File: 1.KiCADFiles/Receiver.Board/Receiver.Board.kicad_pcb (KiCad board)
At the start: 4 copper layers, 251 x 142 mm, 27 parts, among them J4 Conn_01x08, J5 Conn_Coaxial_Out, Q1 MMBT3904, Q2 MMBT3906

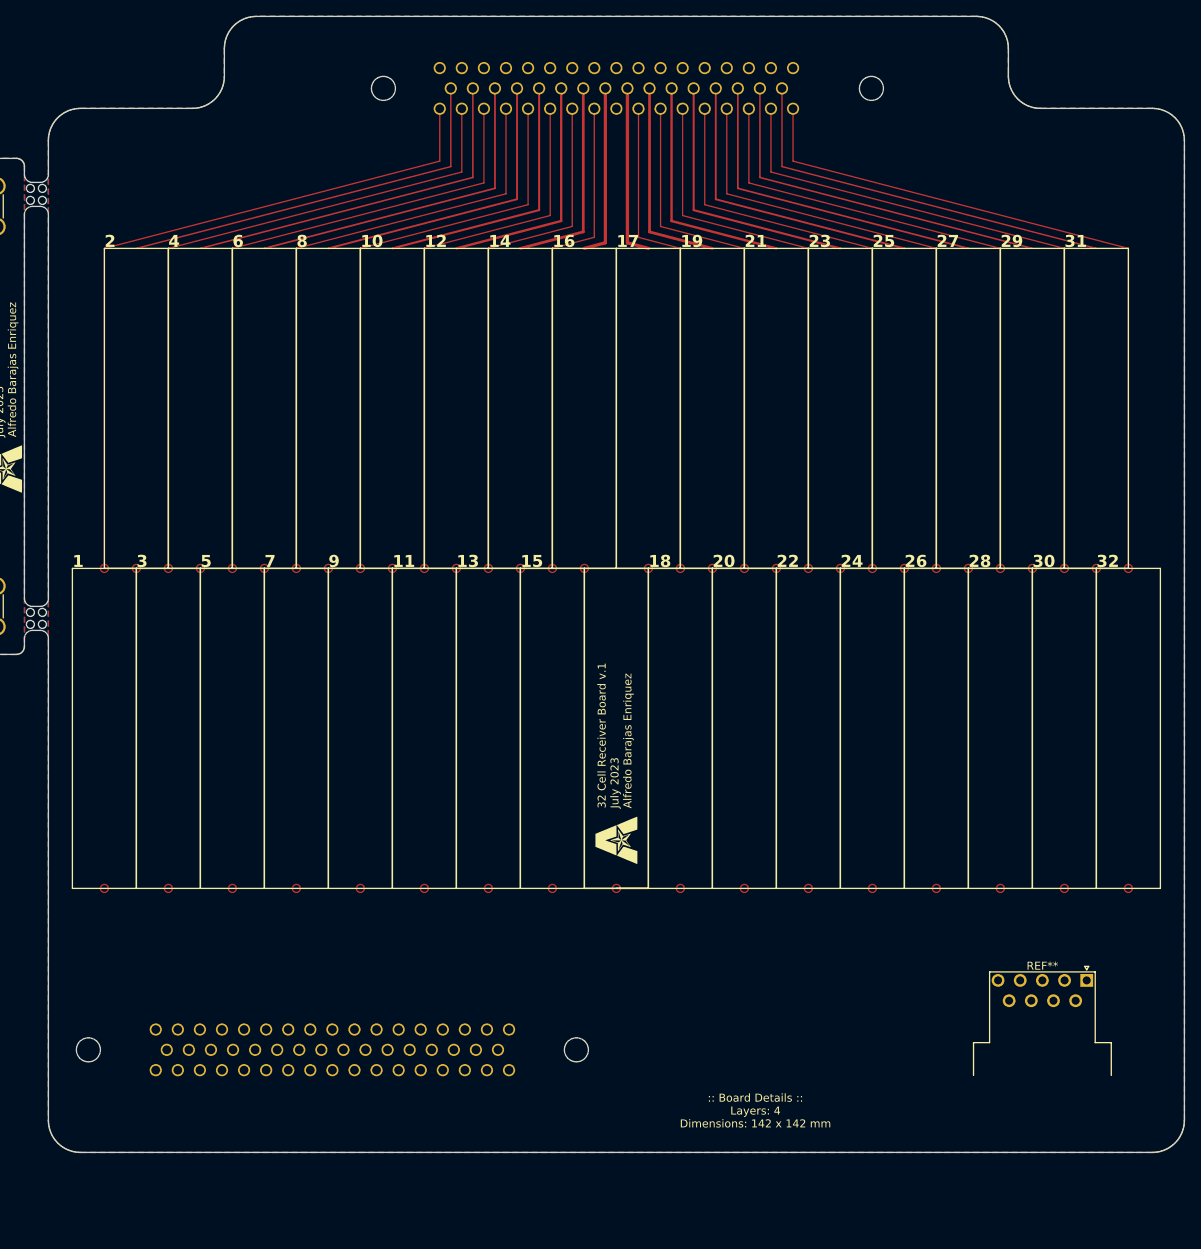
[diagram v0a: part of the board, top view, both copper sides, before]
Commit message: Started signal trace lines
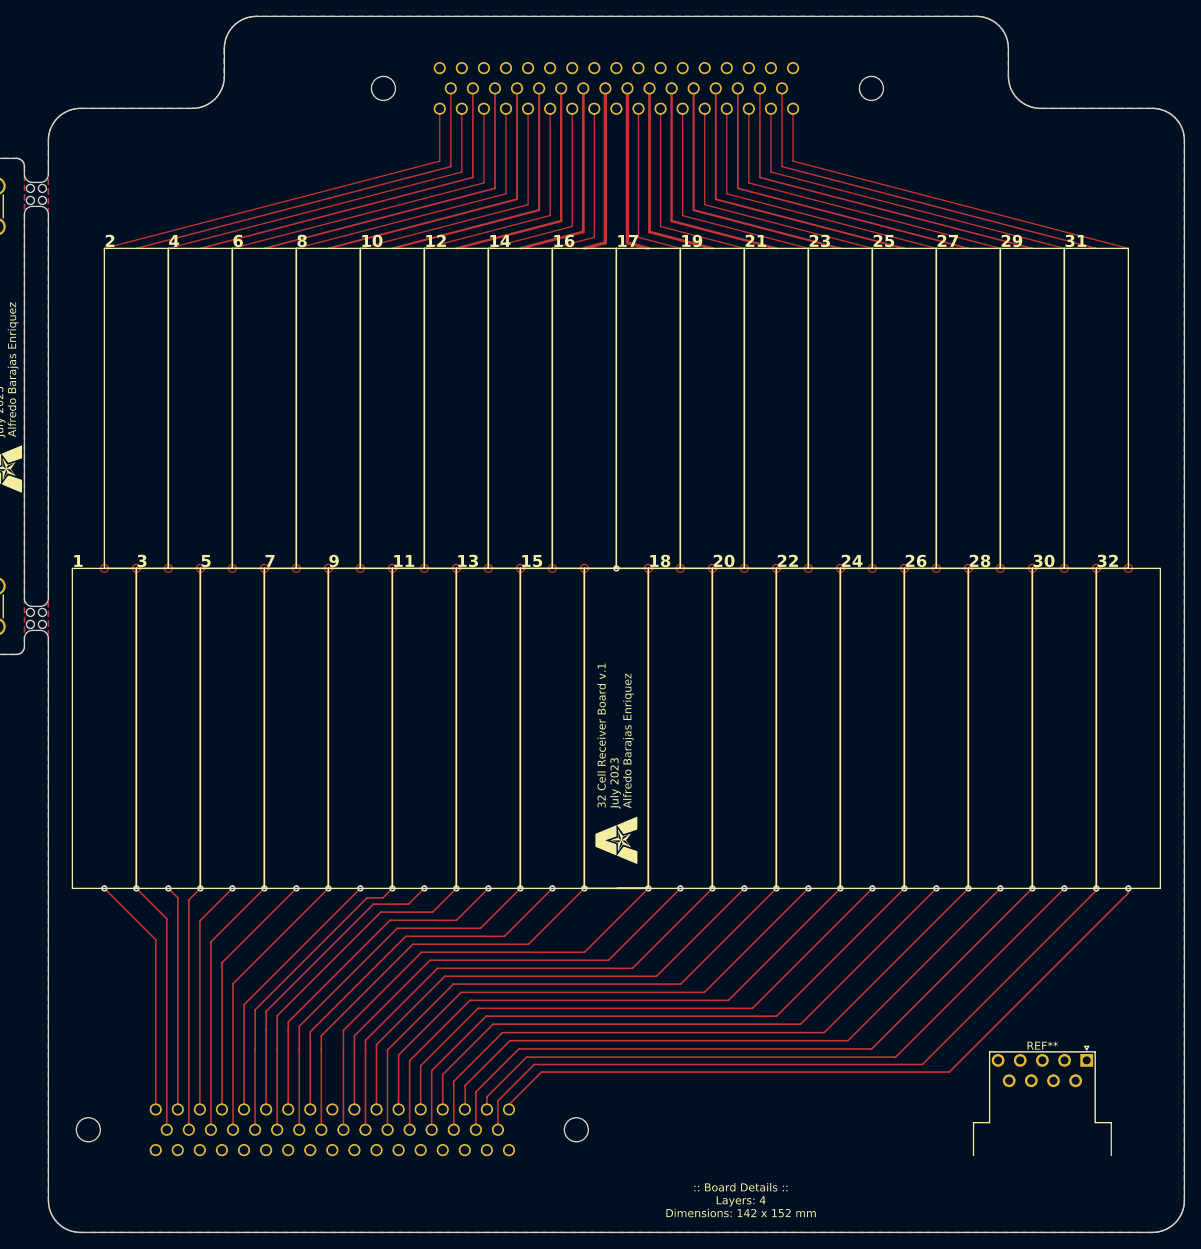
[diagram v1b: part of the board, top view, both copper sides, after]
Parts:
- moved REF** 10.0 mm to (258.8, 181.5)
- moved REF** 9.99 mm to (163.1, 190.2)
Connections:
- D1 pad 2: Net-(D1-A) -> +12
- D2 pad 1: Net-(D2-K) -> -12
- REF** pad 1: (no net) -> GND
- REF** pad 4: (no net) -> +12
- REF** pad 9: (no net) -> -12
- REF** pad 1: Net-(D1-A) -> +12
- REF** pad 3: Net-(D2-K) -> -12
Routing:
- net (no net): track 0.00 -> 1771.0 mm, vias 2 -> 34
- net Net-(D1-A): track 11.6 -> 0.00 mm
- net +12: track 0.00 -> 11.6 mm
- net Net-(D2-K): track 2.88 -> 0.00 mm
- net -12: track 0.00 -> 2.88 mm
- net GND1: vias 0 -> 1
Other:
- board size 251 x 142 mm -> 251 x 152 mm
- board text added: ":: Board Details :: Layers: 4 Dimensions: 142 x 152 mm"
- board text removed: ":: Board Details :: Layers: 4 Dimensions: 142 x 142 mm"

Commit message: Began adding signal traces, added cell holders
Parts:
- removed the REF** at (39.0, 122.1)
- removed the REF** at (39.0, 92.6)
- removed the REF** at (39.0, 89.6)
- removed the REF** at (39.0, 124.6)
- added REF**: PinSocket_1x03_P1.27mm_Vertical, Connector_PinSocket_1.27mm:PinSocket_1x03_P1.27mm_Vertical, F.Cu at (120.6, 114.5)
- added REF**: PinSocket_1x01_P1.27mm_Vertical, Connector_PinSocket_1.27mm:PinSocket_1x01_P1.27mm_Vertical, F.Cu at (120.6, 85.0)
- added REF**: PinSocket_1x01_P1.27mm_Vertical, Connector_PinSocket_1.27mm:PinSocket_1x01_P1.27mm_Vertical, F.Cu at (117.8, 82.5)
- added REF**: PinHeader_1x01_P1.27mm_Horizontal, Connector_PinHeader_1.27mm:PinHeader_1x01_P1.27mm_Horizontal, B.Cu at (39.0, 122.1)
- added REF**: PinHeader_1x03_P1.27mm_Horizontal, Connector_PinHeader_1.27mm:PinHeader_1x03_P1.27mm_Horizontal, B.Cu at (39.0, 95.2)
- added REF**: PinHeader_1x01_P1.27mm_Horizontal, Connector_PinHeader_1.27mm:PinHeader_1x01_P1.27mm_Horizontal, F.Cu at (39.0, 124.6)
- added REF**: PinSocket_1x01_P1.27mm_Vertical, Connector_PinSocket_1.27mm:PinSocket_1x01_P1.27mm_Vertical, F.Cu at (133.6, 157.5)
- added REF**: PinSocket_1x01_P1.27mm_Vertical, Connector_PinSocket_1.27mm:PinSocket_1x01_P1.27mm_Vertical, F.Cu at (136.5, 125.0)
- added REF**: PinSocket_1x01_P1.27mm_Vertical, Connector_PinSocket_1.27mm:PinSocket_1x01_P1.27mm_Vertical, F.Cu at (133.6, 122.5)
- added REF**: PinHeader_1x01_P1.27mm_Horizontal, Connector_PinHeader_1.27mm:PinHeader_1x01_P1.27mm_Horizontal, F.Cu at (39.0, 89.6)
- added REF**: PinSocket_1x01_P1.27mm_Vertical, Connector_PinSocket_1.27mm:PinSocket_1x01_P1.27mm_Vertical, F.Cu at (117.8, 117.5)
- added REF**: PinSocket_1x03_P1.27mm_Vertical, Connector_PinSocket_1.27mm:PinSocket_1x03_P1.27mm_Vertical, F.Cu at (136.5, 154.5)
- added REF**1: PinSocket_1x01_P1.27mm_Vertical, Connector_PinSocket_1.27mm:PinSocket_1x01_P1.27mm_Vertical, F.Cu at (141.6, 157.5)
- added REF**10: PinSocket_1x03_P1.27mm_Vertical, Connector_PinSocket_1.27mm:PinSocket_1x03_P1.27mm_Vertical, F.Cu at (160.5, 154.5)
- added REF**100: PinSocket_1x01_P1.27mm_Vertical, Connector_PinSocket_1.27mm:PinSocket_1x01_P1.27mm_Vertical, F.Cu at (201.6, 82.5)
- added REF**101: PinSocket_1x01_P1.27mm_Vertical, Connector_PinSocket_1.27mm:PinSocket_1x01_P1.27mm_Vertical, F.Cu at (209.6, 117.5)
- added REF**102: PinSocket_1x03_P1.27mm_Vertical, Connector_PinSocket_1.27mm:PinSocket_1x03_P1.27mm_Vertical, F.Cu at (212.5, 114.5)
- added REF**103: PinSocket_1x01_P1.27mm_Vertical, Connector_PinSocket_1.27mm:PinSocket_1x01_P1.27mm_Vertical, F.Cu at (212.5, 85.0)
- added REF**104: PinSocket_1x01_P1.27mm_Vertical, Connector_PinSocket_1.27mm:PinSocket_1x01_P1.27mm_Vertical, F.Cu at (209.6, 82.5)
- added REF**105: PinSocket_1x01_P1.27mm_Vertical, Connector_PinSocket_1.27mm:PinSocket_1x01_P1.27mm_Vertical, F.Cu at (217.6, 117.5)
- added REF**106: PinSocket_1x03_P1.27mm_Vertical, Connector_PinSocket_1.27mm:PinSocket_1x03_P1.27mm_Vertical, F.Cu at (220.5, 114.5)
- added REF**107: PinSocket_1x01_P1.27mm_Vertical, Connector_PinSocket_1.27mm:PinSocket_1x01_P1.27mm_Vertical, F.Cu at (220.5, 85.0)
- added REF**108: PinSocket_1x01_P1.27mm_Vertical, Connector_PinSocket_1.27mm:PinSocket_1x01_P1.27mm_Vertical, F.Cu at (217.6, 82.5)
- added REF**109: PinSocket_1x01_P1.27mm_Vertical, Connector_PinSocket_1.27mm:PinSocket_1x01_P1.27mm_Vertical, F.Cu at (225.6, 117.5)
- added REF**11: PinSocket_1x01_P1.27mm_Vertical, Connector_PinSocket_1.27mm:PinSocket_1x01_P1.27mm_Vertical, F.Cu at (160.5, 125.0)
- added REF**110: PinSocket_1x03_P1.27mm_Vertical, Connector_PinSocket_1.27mm:PinSocket_1x03_P1.27mm_Vertical, F.Cu at (228.5, 114.5)
- added REF**111: PinSocket_1x01_P1.27mm_Vertical, Connector_PinSocket_1.27mm:PinSocket_1x01_P1.27mm_Vertical, F.Cu at (228.5, 85.0)
- added REF**112: PinSocket_1x01_P1.27mm_Vertical, Connector_PinSocket_1.27mm:PinSocket_1x01_P1.27mm_Vertical, F.Cu at (225.6, 82.5)
- added REF**113: PinSocket_1x01_P1.27mm_Vertical, Connector_PinSocket_1.27mm:PinSocket_1x01_P1.27mm_Vertical, F.Cu at (233.6, 117.5)
- added REF**114: PinSocket_1x03_P1.27mm_Vertical, Connector_PinSocket_1.27mm:PinSocket_1x03_P1.27mm_Vertical, F.Cu at (236.5, 114.5)
- added REF**115: PinSocket_1x01_P1.27mm_Vertical, Connector_PinSocket_1.27mm:PinSocket_1x01_P1.27mm_Vertical, F.Cu at (236.5, 85.0)
- added REF**116: PinSocket_1x01_P1.27mm_Vertical, Connector_PinSocket_1.27mm:PinSocket_1x01_P1.27mm_Vertical, F.Cu at (233.6, 82.5)
- added REF**117: PinSocket_1x01_P1.27mm_Vertical, Connector_PinSocket_1.27mm:PinSocket_1x01_P1.27mm_Vertical, F.Cu at (241.6, 117.5)
- added REF**118: PinSocket_1x03_P1.27mm_Vertical, Connector_PinSocket_1.27mm:PinSocket_1x03_P1.27mm_Vertical, F.Cu at (244.5, 114.5)
- added REF**119: PinSocket_1x01_P1.27mm_Vertical, Connector_PinSocket_1.27mm:PinSocket_1x01_P1.27mm_Vertical, F.Cu at (244.5, 85.0)
- added REF**12: PinSocket_1x01_P1.27mm_Vertical, Connector_PinSocket_1.27mm:PinSocket_1x01_P1.27mm_Vertical, F.Cu at (157.6, 122.5)
- added REF**120: PinSocket_1x01_P1.27mm_Vertical, Connector_PinSocket_1.27mm:PinSocket_1x01_P1.27mm_Vertical, F.Cu at (241.6, 82.5)
- added REF**121: PinSocket_1x01_P1.27mm_Vertical, Connector_PinSocket_1.27mm:PinSocket_1x01_P1.27mm_Vertical, F.Cu at (249.6, 117.5)
- added REF**122: PinSocket_1x03_P1.27mm_Vertical, Connector_PinSocket_1.27mm:PinSocket_1x03_P1.27mm_Vertical, F.Cu at (252.5, 114.5)
- added REF**123: PinSocket_1x01_P1.27mm_Vertical, Connector_PinSocket_1.27mm:PinSocket_1x01_P1.27mm_Vertical, F.Cu at (252.5, 85.0)
- added REF**124: PinSocket_1x01_P1.27mm_Vertical, Connector_PinSocket_1.27mm:PinSocket_1x01_P1.27mm_Vertical, F.Cu at (249.6, 82.5)
- added REF**125: PinSocket_1x01_P1.27mm_Vertical, Connector_PinSocket_1.27mm:PinSocket_1x01_P1.27mm_Vertical, F.Cu at (257.6, 117.5)
- added REF**126: PinSocket_1x03_P1.27mm_Vertical, Connector_PinSocket_1.27mm:PinSocket_1x03_P1.27mm_Vertical, F.Cu at (260.5, 114.5)
- added REF**127: PinSocket_1x01_P1.27mm_Vertical, Connector_PinSocket_1.27mm:PinSocket_1x01_P1.27mm_Vertical, F.Cu at (260.5, 85.0)
- added REF**128: PinSocket_1x01_P1.27mm_Vertical, Connector_PinSocket_1.27mm:PinSocket_1x01_P1.27mm_Vertical, F.Cu at (257.6, 82.5)
- added REF**13: PinSocket_1x01_P1.27mm_Vertical, Connector_PinSocket_1.27mm:PinSocket_1x01_P1.27mm_Vertical, F.Cu at (165.6, 157.5)
- added REF**14: PinSocket_1x03_P1.27mm_Vertical, Connector_PinSocket_1.27mm:PinSocket_1x03_P1.27mm_Vertical, F.Cu at (168.5, 154.5)
- added REF**15: PinSocket_1x01_P1.27mm_Vertical, Connector_PinSocket_1.27mm:PinSocket_1x01_P1.27mm_Vertical, F.Cu at (168.5, 125.0)
- added REF**16: PinSocket_1x01_P1.27mm_Vertical, Connector_PinSocket_1.27mm:PinSocket_1x01_P1.27mm_Vertical, F.Cu at (165.6, 122.5)
- added REF**17: PinSocket_1x01_P1.27mm_Vertical, Connector_PinSocket_1.27mm:PinSocket_1x01_P1.27mm_Vertical, F.Cu at (173.6, 157.5)
- added REF**18: PinSocket_1x03_P1.27mm_Vertical, Connector_PinSocket_1.27mm:PinSocket_1x03_P1.27mm_Vertical, F.Cu at (176.5, 154.5)
- added REF**19: PinSocket_1x01_P1.27mm_Vertical, Connector_PinSocket_1.27mm:PinSocket_1x01_P1.27mm_Vertical, F.Cu at (176.5, 125.0)
- added REF**2: PinSocket_1x03_P1.27mm_Vertical, Connector_PinSocket_1.27mm:PinSocket_1x03_P1.27mm_Vertical, F.Cu at (144.5, 154.5)
- added REF**20: PinSocket_1x01_P1.27mm_Vertical, Connector_PinSocket_1.27mm:PinSocket_1x01_P1.27mm_Vertical, F.Cu at (173.6, 122.5)
- added REF**21: PinSocket_1x01_P1.27mm_Vertical, Connector_PinSocket_1.27mm:PinSocket_1x01_P1.27mm_Vertical, F.Cu at (181.6, 157.5)
- added REF**22: PinSocket_1x03_P1.27mm_Vertical, Connector_PinSocket_1.27mm:PinSocket_1x03_P1.27mm_Vertical, F.Cu at (184.5, 154.5)
- added REF**23: PinSocket_1x01_P1.27mm_Vertical, Connector_PinSocket_1.27mm:PinSocket_1x01_P1.27mm_Vertical, F.Cu at (184.5, 125.0)
- added REF**24: PinSocket_1x01_P1.27mm_Vertical, Connector_PinSocket_1.27mm:PinSocket_1x01_P1.27mm_Vertical, F.Cu at (181.6, 122.5)
- added REF**25: PinSocket_1x01_P1.27mm_Vertical, Connector_PinSocket_1.27mm:PinSocket_1x01_P1.27mm_Vertical, F.Cu at (189.6, 157.5)
- added REF**26: PinSocket_1x03_P1.27mm_Vertical, Connector_PinSocket_1.27mm:PinSocket_1x03_P1.27mm_Vertical, F.Cu at (192.5, 154.5)
- added REF**27: PinSocket_1x01_P1.27mm_Vertical, Connector_PinSocket_1.27mm:PinSocket_1x01_P1.27mm_Vertical, F.Cu at (192.5, 125.0)
- added REF**28: PinSocket_1x01_P1.27mm_Vertical, Connector_PinSocket_1.27mm:PinSocket_1x01_P1.27mm_Vertical, F.Cu at (189.6, 122.5)
- added REF**3: PinSocket_1x01_P1.27mm_Vertical, Connector_PinSocket_1.27mm:PinSocket_1x01_P1.27mm_Vertical, F.Cu at (144.5, 125.0)
- added REF**33: PinSocket_1x01_P1.27mm_Vertical, Connector_PinSocket_1.27mm:PinSocket_1x01_P1.27mm_Vertical, F.Cu at (205.6, 157.5)
- added REF**34: PinSocket_1x03_P1.27mm_Vertical, Connector_PinSocket_1.27mm:PinSocket_1x03_P1.27mm_Vertical, F.Cu at (208.5, 154.5)
- added REF**35: PinSocket_1x01_P1.27mm_Vertical, Connector_PinSocket_1.27mm:PinSocket_1x01_P1.27mm_Vertical, F.Cu at (208.5, 125.0)
- added REF**36: PinSocket_1x01_P1.27mm_Vertical, Connector_PinSocket_1.27mm:PinSocket_1x01_P1.27mm_Vertical, F.Cu at (205.6, 122.5)
- added REF**37: PinSocket_1x01_P1.27mm_Vertical, Connector_PinSocket_1.27mm:PinSocket_1x01_P1.27mm_Vertical, F.Cu at (213.6, 157.5)
- added REF**38: PinSocket_1x03_P1.27mm_Vertical, Connector_PinSocket_1.27mm:PinSocket_1x03_P1.27mm_Vertical, F.Cu at (216.5, 154.5)
- added REF**39: PinSocket_1x01_P1.27mm_Vertical, Connector_PinSocket_1.27mm:PinSocket_1x01_P1.27mm_Vertical, F.Cu at (216.5, 125.0)
- added REF**4: PinSocket_1x01_P1.27mm_Vertical, Connector_PinSocket_1.27mm:PinSocket_1x01_P1.27mm_Vertical, F.Cu at (141.6, 122.5)
- added REF**40: PinSocket_1x01_P1.27mm_Vertical, Connector_PinSocket_1.27mm:PinSocket_1x01_P1.27mm_Vertical, F.Cu at (213.6, 122.5)
- added REF**41: PinSocket_1x01_P1.27mm_Vertical, Connector_PinSocket_1.27mm:PinSocket_1x01_P1.27mm_Vertical, F.Cu at (221.6, 157.5)
- added REF**42: PinSocket_1x03_P1.27mm_Vertical, Connector_PinSocket_1.27mm:PinSocket_1x03_P1.27mm_Vertical, F.Cu at (224.5, 154.5)
- added REF**43: PinSocket_1x01_P1.27mm_Vertical, Connector_PinSocket_1.27mm:PinSocket_1x01_P1.27mm_Vertical, F.Cu at (224.5, 125.0)
- added REF**44: PinSocket_1x01_P1.27mm_Vertical, Connector_PinSocket_1.27mm:PinSocket_1x01_P1.27mm_Vertical, F.Cu at (221.6, 122.5)
- added REF**45: PinSocket_1x01_P1.27mm_Vertical, Connector_PinSocket_1.27mm:PinSocket_1x01_P1.27mm_Vertical, F.Cu at (229.6, 157.5)
- added REF**46: PinSocket_1x03_P1.27mm_Vertical, Connector_PinSocket_1.27mm:PinSocket_1x03_P1.27mm_Vertical, F.Cu at (232.5, 154.5)
- added REF**47: PinSocket_1x01_P1.27mm_Vertical, Connector_PinSocket_1.27mm:PinSocket_1x01_P1.27mm_Vertical, F.Cu at (232.5, 125.0)
- added REF**48: PinSocket_1x01_P1.27mm_Vertical, Connector_PinSocket_1.27mm:PinSocket_1x01_P1.27mm_Vertical, F.Cu at (229.6, 122.5)
- added REF**49: PinSocket_1x01_P1.27mm_Vertical, Connector_PinSocket_1.27mm:PinSocket_1x01_P1.27mm_Vertical, F.Cu at (237.6, 157.5)
- added REF**5: PinSocket_1x01_P1.27mm_Vertical, Connector_PinSocket_1.27mm:PinSocket_1x01_P1.27mm_Vertical, F.Cu at (149.6, 157.5)
- added REF**50: PinSocket_1x03_P1.27mm_Vertical, Connector_PinSocket_1.27mm:PinSocket_1x03_P1.27mm_Vertical, F.Cu at (240.5, 154.5)
- added REF**51: PinSocket_1x01_P1.27mm_Vertical, Connector_PinSocket_1.27mm:PinSocket_1x01_P1.27mm_Vertical, F.Cu at (240.5, 125.0)
- added REF**52: PinSocket_1x01_P1.27mm_Vertical, Connector_PinSocket_1.27mm:PinSocket_1x01_P1.27mm_Vertical, F.Cu at (237.6, 122.5)
- added REF**53: PinSocket_1x01_P1.27mm_Vertical, Connector_PinSocket_1.27mm:PinSocket_1x01_P1.27mm_Vertical, F.Cu at (245.6, 157.5)
- added REF**54: PinSocket_1x03_P1.27mm_Vertical, Connector_PinSocket_1.27mm:PinSocket_1x03_P1.27mm_Vertical, F.Cu at (248.5, 154.5)
- added REF**55: PinSocket_1x01_P1.27mm_Vertical, Connector_PinSocket_1.27mm:PinSocket_1x01_P1.27mm_Vertical, F.Cu at (248.5, 125.0)
- added REF**56: PinSocket_1x01_P1.27mm_Vertical, Connector_PinSocket_1.27mm:PinSocket_1x01_P1.27mm_Vertical, F.Cu at (245.6, 122.5)
- added REF**57: PinSocket_1x01_P1.27mm_Vertical, Connector_PinSocket_1.27mm:PinSocket_1x01_P1.27mm_Vertical, F.Cu at (253.6, 157.5)
- added REF**58: PinSocket_1x03_P1.27mm_Vertical, Connector_PinSocket_1.27mm:PinSocket_1x03_P1.27mm_Vertical, F.Cu at (256.5, 154.5)
- added REF**59: PinSocket_1x01_P1.27mm_Vertical, Connector_PinSocket_1.27mm:PinSocket_1x01_P1.27mm_Vertical, F.Cu at (256.5, 125.0)
- added REF**6: PinSocket_1x03_P1.27mm_Vertical, Connector_PinSocket_1.27mm:PinSocket_1x03_P1.27mm_Vertical, F.Cu at (152.5, 154.5)
- added REF**60: PinSocket_1x01_P1.27mm_Vertical, Connector_PinSocket_1.27mm:PinSocket_1x01_P1.27mm_Vertical, F.Cu at (253.6, 122.5)
- added REF**61: PinSocket_1x01_P1.27mm_Vertical, Connector_PinSocket_1.27mm:PinSocket_1x01_P1.27mm_Vertical, F.Cu at (261.6, 157.5)
- added REF**62: PinSocket_1x03_P1.27mm_Vertical, Connector_PinSocket_1.27mm:PinSocket_1x03_P1.27mm_Vertical, F.Cu at (264.5, 154.5)
- added REF**63: PinSocket_1x01_P1.27mm_Vertical, Connector_PinSocket_1.27mm:PinSocket_1x01_P1.27mm_Vertical, F.Cu at (264.5, 125.0)
- added REF**64: PinSocket_1x01_P1.27mm_Vertical, Connector_PinSocket_1.27mm:PinSocket_1x01_P1.27mm_Vertical, F.Cu at (261.6, 122.5)
- added REF**65: PinSocket_1x01_P1.27mm_Vertical, Connector_PinSocket_1.27mm:PinSocket_1x01_P1.27mm_Vertical, F.Cu at (137.6, 117.5)
- added REF**66: PinSocket_1x03_P1.27mm_Vertical, Connector_PinSocket_1.27mm:PinSocket_1x03_P1.27mm_Vertical, F.Cu at (140.5, 114.5)
- added REF**67: PinSocket_1x01_P1.27mm_Vertical, Connector_PinSocket_1.27mm:PinSocket_1x01_P1.27mm_Vertical, F.Cu at (140.5, 85.0)
- added REF**68: PinSocket_1x01_P1.27mm_Vertical, Connector_PinSocket_1.27mm:PinSocket_1x01_P1.27mm_Vertical, F.Cu at (137.6, 82.5)
- added REF**69: PinSocket_1x01_P1.27mm_Vertical, Connector_PinSocket_1.27mm:PinSocket_1x01_P1.27mm_Vertical, F.Cu at (145.6, 117.5)
- added REF**7: PinSocket_1x01_P1.27mm_Vertical, Connector_PinSocket_1.27mm:PinSocket_1x01_P1.27mm_Vertical, F.Cu at (152.5, 125.0)
- added REF**70: PinSocket_1x03_P1.27mm_Vertical, Connector_PinSocket_1.27mm:PinSocket_1x03_P1.27mm_Vertical, F.Cu at (148.5, 114.5)
- added REF**71: PinSocket_1x01_P1.27mm_Vertical, Connector_PinSocket_1.27mm:PinSocket_1x01_P1.27mm_Vertical, F.Cu at (148.5, 85.0)
- added REF**72: PinSocket_1x01_P1.27mm_Vertical, Connector_PinSocket_1.27mm:PinSocket_1x01_P1.27mm_Vertical, F.Cu at (145.6, 82.5)
- added REF**73: PinSocket_1x01_P1.27mm_Vertical, Connector_PinSocket_1.27mm:PinSocket_1x01_P1.27mm_Vertical, F.Cu at (153.6, 117.5)
- added REF**74: PinSocket_1x03_P1.27mm_Vertical, Connector_PinSocket_1.27mm:PinSocket_1x03_P1.27mm_Vertical, F.Cu at (156.5, 114.5)
- added REF**75: PinSocket_1x01_P1.27mm_Vertical, Connector_PinSocket_1.27mm:PinSocket_1x01_P1.27mm_Vertical, F.Cu at (156.5, 85.0)
- added REF**76: PinSocket_1x01_P1.27mm_Vertical, Connector_PinSocket_1.27mm:PinSocket_1x01_P1.27mm_Vertical, F.Cu at (153.6, 82.5)
- added REF**77: PinSocket_1x01_P1.27mm_Vertical, Connector_PinSocket_1.27mm:PinSocket_1x01_P1.27mm_Vertical, F.Cu at (161.6, 117.5)
- added REF**78: PinSocket_1x03_P1.27mm_Vertical, Connector_PinSocket_1.27mm:PinSocket_1x03_P1.27mm_Vertical, F.Cu at (164.5, 114.5)
- added REF**79: PinSocket_1x01_P1.27mm_Vertical, Connector_PinSocket_1.27mm:PinSocket_1x01_P1.27mm_Vertical, F.Cu at (164.5, 85.0)
- added REF**8: PinSocket_1x01_P1.27mm_Vertical, Connector_PinSocket_1.27mm:PinSocket_1x01_P1.27mm_Vertical, F.Cu at (149.6, 122.5)
- added REF**80: PinSocket_1x01_P1.27mm_Vertical, Connector_PinSocket_1.27mm:PinSocket_1x01_P1.27mm_Vertical, F.Cu at (161.6, 82.5)
- added REF**81: PinSocket_1x01_P1.27mm_Vertical, Connector_PinSocket_1.27mm:PinSocket_1x01_P1.27mm_Vertical, F.Cu at (169.6, 117.5)
- added REF**82: PinSocket_1x03_P1.27mm_Vertical, Connector_PinSocket_1.27mm:PinSocket_1x03_P1.27mm_Vertical, F.Cu at (172.5, 114.5)
- added REF**83: PinSocket_1x01_P1.27mm_Vertical, Connector_PinSocket_1.27mm:PinSocket_1x01_P1.27mm_Vertical, F.Cu at (172.5, 85.0)
- added REF**84: PinSocket_1x01_P1.27mm_Vertical, Connector_PinSocket_1.27mm:PinSocket_1x01_P1.27mm_Vertical, F.Cu at (169.6, 82.5)
- added REF**85: PinSocket_1x01_P1.27mm_Vertical, Connector_PinSocket_1.27mm:PinSocket_1x01_P1.27mm_Vertical, F.Cu at (177.6, 117.5)
- added REF**86: PinSocket_1x03_P1.27mm_Vertical, Connector_PinSocket_1.27mm:PinSocket_1x03_P1.27mm_Vertical, F.Cu at (180.5, 114.5)
- added REF**87: PinSocket_1x01_P1.27mm_Vertical, Connector_PinSocket_1.27mm:PinSocket_1x01_P1.27mm_Vertical, F.Cu at (180.5, 85.0)
- added REF**88: PinSocket_1x01_P1.27mm_Vertical, Connector_PinSocket_1.27mm:PinSocket_1x01_P1.27mm_Vertical, F.Cu at (177.6, 82.5)
- added REF**89: PinSocket_1x01_P1.27mm_Vertical, Connector_PinSocket_1.27mm:PinSocket_1x01_P1.27mm_Vertical, F.Cu at (185.6, 117.5)
- added REF**9: PinSocket_1x01_P1.27mm_Vertical, Connector_PinSocket_1.27mm:PinSocket_1x01_P1.27mm_Vertical, F.Cu at (157.6, 157.5)
- added REF**90: PinSocket_1x03_P1.27mm_Vertical, Connector_PinSocket_1.27mm:PinSocket_1x03_P1.27mm_Vertical, F.Cu at (188.5, 114.5)
- added REF**91: PinSocket_1x01_P1.27mm_Vertical, Connector_PinSocket_1.27mm:PinSocket_1x01_P1.27mm_Vertical, F.Cu at (188.5, 85.0)
- added REF**92: PinSocket_1x01_P1.27mm_Vertical, Connector_PinSocket_1.27mm:PinSocket_1x01_P1.27mm_Vertical, F.Cu at (185.6, 82.5)
- added REF**93: PinSocket_1x01_P1.27mm_Vertical, Connector_PinSocket_1.27mm:PinSocket_1x01_P1.27mm_Vertical, F.Cu at (193.6, 117.5)
- added REF**94: PinSocket_1x03_P1.27mm_Vertical, Connector_PinSocket_1.27mm:PinSocket_1x03_P1.27mm_Vertical, F.Cu at (196.5, 114.5)
- added REF**95: PinSocket_1x01_P1.27mm_Vertical, Connector_PinSocket_1.27mm:PinSocket_1x01_P1.27mm_Vertical, F.Cu at (196.5, 85.0)
- added REF**96: PinSocket_1x01_P1.27mm_Vertical, Connector_PinSocket_1.27mm:PinSocket_1x01_P1.27mm_Vertical, F.Cu at (193.6, 82.5)
- added REF**97: PinSocket_1x01_P1.27mm_Vertical, Connector_PinSocket_1.27mm:PinSocket_1x01_P1.27mm_Vertical, F.Cu at (201.6, 117.5)
- added REF**98: PinSocket_1x03_P1.27mm_Vertical, Connector_PinSocket_1.27mm:PinSocket_1x03_P1.27mm_Vertical, F.Cu at (204.5, 114.5)
- added REF**99: PinSocket_1x01_P1.27mm_Vertical, Connector_PinSocket_1.27mm:PinSocket_1x01_P1.27mm_Vertical, F.Cu at (204.5, 85.0)
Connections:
- REF** pad 1: (no net) -> GND
- REF** pad 4: (no net) -> +12
- REF** pad 8: (no net) -> -12
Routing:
- net (no net): track 1771.0 -> 1813.1 mm, vias 34 -> 2
- net +12: track 11.6 -> 41.9 mm
- net -12: track 2.88 -> 28.6 mm

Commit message: Fixed cell board orientation, routed power lines, fixed wire capacitance with new lengths, updated excel sheet to include all traces
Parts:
- removed C1, C2, C3, C4: 10uF, Capacitor_SMD:C_1206_3216Metric_Pad1.33x1.80mm_HandSolder
- removed D1, D2: 1N4148W, Diode_SMD:D_SOD-123
- removed D3, D4: BZV55B7V5, Diode_SMD:D_MiniMELF
- removed J4: Conn_01x08, Connector_PinSocket_2.54mm:PinSocket_1x08_P2.54mm_Vertical
- removed Q1: MMBT3904, Package_TO_SOT_SMD:SOT-23
- removed Q2: MMBT3906, Package_TO_SOT_SMD:SOT-23
- removed R1, R2: 1.0k, Resistor_SMD:R_1206_3216Metric_Pad1.30x1.75mm_HandSolder
- removed R3, R4: 4.7, Resistor_SMD:R_1206_3216Metric_Pad1.30x1.75mm_HandSolder
- removed the REF** at (39.0, 122.1)
- removed the REF** at (39.0, 95.2)
- removed the REF** at (39.0, 124.6)
- removed the REF** at (39.0, 89.6)
- added REF**: R_1206_3216Metric_Pad1.30x1.75mm_HandSolder, Resistor_SMD:R_1206_3216Metric_Pad1.30x1.75mm_HandSolder, B.Cu at (140.5, 108.9)
- added REF**: R_1206_3216Metric_Pad1.30x1.75mm_HandSolder, Resistor_SMD:R_1206_3216Metric_Pad1.30x1.75mm_HandSolder, B.Cu at (140.5, 117.5)
- added REF**129: R_1206_3216Metric_Pad1.30x1.75mm_HandSolder, Resistor_SMD:R_1206_3216Metric_Pad1.30x1.75mm_HandSolder, B.Cu at (164.5, 117.5)
- added REF**130: R_1206_3216Metric_Pad1.30x1.75mm_HandSolder, Resistor_SMD:R_1206_3216Metric_Pad1.30x1.75mm_HandSolder, B.Cu at (164.5, 108.9)
- added REF**131: R_1206_3216Metric_Pad1.30x1.75mm_HandSolder, Resistor_SMD:R_1206_3216Metric_Pad1.30x1.75mm_HandSolder, B.Cu at (172.5, 117.5)
- added REF**132: R_1206_3216Metric_Pad1.30x1.75mm_HandSolder, Resistor_SMD:R_1206_3216Metric_Pad1.30x1.75mm_HandSolder, B.Cu at (172.5, 108.9)
- added REF**133: R_1206_3216Metric_Pad1.30x1.75mm_HandSolder, Resistor_SMD:R_1206_3216Metric_Pad1.30x1.75mm_HandSolder, B.Cu at (180.5, 117.5)
- added REF**134: R_1206_3216Metric_Pad1.30x1.75mm_HandSolder, Resistor_SMD:R_1206_3216Metric_Pad1.30x1.75mm_HandSolder, B.Cu at (180.5, 108.9)
- added REF**135: R_1206_3216Metric_Pad1.30x1.75mm_HandSolder, Resistor_SMD:R_1206_3216Metric_Pad1.30x1.75mm_HandSolder, B.Cu at (188.5, 117.5)
- added REF**136: R_1206_3216Metric_Pad1.30x1.75mm_HandSolder, Resistor_SMD:R_1206_3216Metric_Pad1.30x1.75mm_HandSolder, B.Cu at (188.5, 108.9)
- added REF**137: R_1206_3216Metric_Pad1.30x1.75mm_HandSolder, Resistor_SMD:R_1206_3216Metric_Pad1.30x1.75mm_HandSolder, B.Cu at (196.5, 117.5)
- added REF**138: R_1206_3216Metric_Pad1.30x1.75mm_HandSolder, Resistor_SMD:R_1206_3216Metric_Pad1.30x1.75mm_HandSolder, B.Cu at (196.5, 108.9)
- added REF**139: R_1206_3216Metric_Pad1.30x1.75mm_HandSolder, Resistor_SMD:R_1206_3216Metric_Pad1.30x1.75mm_HandSolder, B.Cu at (204.5, 117.5)
- added REF**140: R_1206_3216Metric_Pad1.30x1.75mm_HandSolder, Resistor_SMD:R_1206_3216Metric_Pad1.30x1.75mm_HandSolder, B.Cu at (204.5, 108.9)
- added REF**141: R_1206_3216Metric_Pad1.30x1.75mm_HandSolder, Resistor_SMD:R_1206_3216Metric_Pad1.30x1.75mm_HandSolder, B.Cu at (212.5, 117.5)
- added REF**142: R_1206_3216Metric_Pad1.30x1.75mm_HandSolder, Resistor_SMD:R_1206_3216Metric_Pad1.30x1.75mm_HandSolder, B.Cu at (212.5, 108.9)
- added REF**143: R_1206_3216Metric_Pad1.30x1.75mm_HandSolder, Resistor_SMD:R_1206_3216Metric_Pad1.30x1.75mm_HandSolder, B.Cu at (220.5, 117.5)
- added REF**144: R_1206_3216Metric_Pad1.30x1.75mm_HandSolder, Resistor_SMD:R_1206_3216Metric_Pad1.30x1.75mm_HandSolder, B.Cu at (220.5, 108.9)
- added REF**145: R_1206_3216Metric_Pad1.30x1.75mm_HandSolder, Resistor_SMD:R_1206_3216Metric_Pad1.30x1.75mm_HandSolder, B.Cu at (228.5, 117.5)
- added REF**146: R_1206_3216Metric_Pad1.30x1.75mm_HandSolder, Resistor_SMD:R_1206_3216Metric_Pad1.30x1.75mm_HandSolder, B.Cu at (228.5, 108.9)
- added REF**147: R_1206_3216Metric_Pad1.30x1.75mm_HandSolder, Resistor_SMD:R_1206_3216Metric_Pad1.30x1.75mm_HandSolder, B.Cu at (236.5, 117.5)
- added REF**148: R_1206_3216Metric_Pad1.30x1.75mm_HandSolder, Resistor_SMD:R_1206_3216Metric_Pad1.30x1.75mm_HandSolder, B.Cu at (236.5, 108.9)
- added REF**149: R_1206_3216Metric_Pad1.30x1.75mm_HandSolder, Resistor_SMD:R_1206_3216Metric_Pad1.30x1.75mm_HandSolder, B.Cu at (244.5, 117.5)
- added REF**150: R_1206_3216Metric_Pad1.30x1.75mm_HandSolder, Resistor_SMD:R_1206_3216Metric_Pad1.30x1.75mm_HandSolder, B.Cu at (244.5, 108.9)
- added REF**151: R_1206_3216Metric_Pad1.30x1.75mm_HandSolder, Resistor_SMD:R_1206_3216Metric_Pad1.30x1.75mm_HandSolder, B.Cu at (252.5, 117.5)
- added REF**152: R_1206_3216Metric_Pad1.30x1.75mm_HandSolder, Resistor_SMD:R_1206_3216Metric_Pad1.30x1.75mm_HandSolder, B.Cu at (252.5, 108.9)
- added REF**153: R_1206_3216Metric_Pad1.30x1.75mm_HandSolder, Resistor_SMD:R_1206_3216Metric_Pad1.30x1.75mm_HandSolder, B.Cu at (260.5, 117.5)
- added REF**154: R_1206_3216Metric_Pad1.30x1.75mm_HandSolder, Resistor_SMD:R_1206_3216Metric_Pad1.30x1.75mm_HandSolder, B.Cu at (260.5, 108.9)
- added REF**155: R_1206_3216Metric_Pad1.30x1.75mm_HandSolder, Resistor_SMD:R_1206_3216Metric_Pad1.30x1.75mm_HandSolder, B.Cu at (144.5, 157.6)
- added REF**156: R_1206_3216Metric_Pad1.30x1.75mm_HandSolder, Resistor_SMD:R_1206_3216Metric_Pad1.30x1.75mm_HandSolder, B.Cu at (144.5, 148.9)
- added REF**157: R_1206_3216Metric_Pad1.30x1.75mm_HandSolder, Resistor_SMD:R_1206_3216Metric_Pad1.30x1.75mm_HandSolder, B.Cu at (152.5, 157.6)
- added REF**158: R_1206_3216Metric_Pad1.30x1.75mm_HandSolder, Resistor_SMD:R_1206_3216Metric_Pad1.30x1.75mm_HandSolder, B.Cu at (152.5, 148.9)
- added REF**159: R_1206_3216Metric_Pad1.30x1.75mm_HandSolder, Resistor_SMD:R_1206_3216Metric_Pad1.30x1.75mm_HandSolder, B.Cu at (160.5, 157.6)
- added REF**160: R_1206_3216Metric_Pad1.30x1.75mm_HandSolder, Resistor_SMD:R_1206_3216Metric_Pad1.30x1.75mm_HandSolder, B.Cu at (160.5, 148.9)
- added REF**161: R_1206_3216Metric_Pad1.30x1.75mm_HandSolder, Resistor_SMD:R_1206_3216Metric_Pad1.30x1.75mm_HandSolder, B.Cu at (168.5, 157.6)
- added REF**162: R_1206_3216Metric_Pad1.30x1.75mm_HandSolder, Resistor_SMD:R_1206_3216Metric_Pad1.30x1.75mm_HandSolder, B.Cu at (168.5, 148.9)
- added REF**163: R_1206_3216Metric_Pad1.30x1.75mm_HandSolder, Resistor_SMD:R_1206_3216Metric_Pad1.30x1.75mm_HandSolder, B.Cu at (176.5, 157.6)
- added REF**164: R_1206_3216Metric_Pad1.30x1.75mm_HandSolder, Resistor_SMD:R_1206_3216Metric_Pad1.30x1.75mm_HandSolder, B.Cu at (176.5, 148.9)
- added REF**165: R_1206_3216Metric_Pad1.30x1.75mm_HandSolder, Resistor_SMD:R_1206_3216Metric_Pad1.30x1.75mm_HandSolder, B.Cu at (184.5, 157.6)
- added REF**166: R_1206_3216Metric_Pad1.30x1.75mm_HandSolder, Resistor_SMD:R_1206_3216Metric_Pad1.30x1.75mm_HandSolder, B.Cu at (184.5, 148.9)
- added REF**167: R_1206_3216Metric_Pad1.30x1.75mm_HandSolder, Resistor_SMD:R_1206_3216Metric_Pad1.30x1.75mm_HandSolder, B.Cu at (192.5, 157.6)
- added REF**168: R_1206_3216Metric_Pad1.30x1.75mm_HandSolder, Resistor_SMD:R_1206_3216Metric_Pad1.30x1.75mm_HandSolder, B.Cu at (192.5, 148.9)
- added REF**171: R_1206_3216Metric_Pad1.30x1.75mm_HandSolder, Resistor_SMD:R_1206_3216Metric_Pad1.30x1.75mm_HandSolder, B.Cu at (208.5, 157.6)
- added REF**172: R_1206_3216Metric_Pad1.30x1.75mm_HandSolder, Resistor_SMD:R_1206_3216Metric_Pad1.30x1.75mm_HandSolder, B.Cu at (208.5, 148.9)
- added REF**173: R_1206_3216Metric_Pad1.30x1.75mm_HandSolder, Resistor_SMD:R_1206_3216Metric_Pad1.30x1.75mm_HandSolder, B.Cu at (216.5, 157.6)
- added REF**174: R_1206_3216Metric_Pad1.30x1.75mm_HandSolder, Resistor_SMD:R_1206_3216Metric_Pad1.30x1.75mm_HandSolder, B.Cu at (216.5, 148.9)
- added REF**175: R_1206_3216Metric_Pad1.30x1.75mm_HandSolder, Resistor_SMD:R_1206_3216Metric_Pad1.30x1.75mm_HandSolder, B.Cu at (224.5, 157.6)
- added REF**176: R_1206_3216Metric_Pad1.30x1.75mm_HandSolder, Resistor_SMD:R_1206_3216Metric_Pad1.30x1.75mm_HandSolder, B.Cu at (224.5, 148.9)
- added REF**177: R_1206_3216Metric_Pad1.30x1.75mm_HandSolder, Resistor_SMD:R_1206_3216Metric_Pad1.30x1.75mm_HandSolder, B.Cu at (232.5, 157.6)
- added REF**178: R_1206_3216Metric_Pad1.30x1.75mm_HandSolder, Resistor_SMD:R_1206_3216Metric_Pad1.30x1.75mm_HandSolder, B.Cu at (232.5, 148.9)
- added REF**179: R_1206_3216Metric_Pad1.30x1.75mm_HandSolder, Resistor_SMD:R_1206_3216Metric_Pad1.30x1.75mm_HandSolder, B.Cu at (240.5, 157.6)
- added REF**180: R_1206_3216Metric_Pad1.30x1.75mm_HandSolder, Resistor_SMD:R_1206_3216Metric_Pad1.30x1.75mm_HandSolder, B.Cu at (240.5, 148.9)
- added REF**181: R_1206_3216Metric_Pad1.30x1.75mm_HandSolder, Resistor_SMD:R_1206_3216Metric_Pad1.30x1.75mm_HandSolder, B.Cu at (248.5, 157.6)
- added REF**182: R_1206_3216Metric_Pad1.30x1.75mm_HandSolder, Resistor_SMD:R_1206_3216Metric_Pad1.30x1.75mm_HandSolder, B.Cu at (248.5, 148.9)
- added REF**183: R_1206_3216Metric_Pad1.30x1.75mm_HandSolder, Resistor_SMD:R_1206_3216Metric_Pad1.30x1.75mm_HandSolder, B.Cu at (256.5, 157.6)
- added REF**184: R_1206_3216Metric_Pad1.30x1.75mm_HandSolder, Resistor_SMD:R_1206_3216Metric_Pad1.30x1.75mm_HandSolder, B.Cu at (256.5, 148.9)
- added REF**185: R_1206_3216Metric_Pad1.30x1.75mm_HandSolder, Resistor_SMD:R_1206_3216Metric_Pad1.30x1.75mm_HandSolder, B.Cu at (264.5, 157.6)
- added REF**186: R_1206_3216Metric_Pad1.30x1.75mm_HandSolder, Resistor_SMD:R_1206_3216Metric_Pad1.30x1.75mm_HandSolder, B.Cu at (264.5, 148.9)
- added REF**187: R_1206_3216Metric_Pad1.30x1.75mm_HandSolder, Resistor_SMD:R_1206_3216Metric_Pad1.30x1.75mm_HandSolder, B.Cu at (136.5, 157.6)
- added REF**188: R_1206_3216Metric_Pad1.30x1.75mm_HandSolder, Resistor_SMD:R_1206_3216Metric_Pad1.30x1.75mm_HandSolder, B.Cu at (136.5, 148.9)
- added REF**29: R_1206_3216Metric_Pad1.30x1.75mm_HandSolder, Resistor_SMD:R_1206_3216Metric_Pad1.30x1.75mm_HandSolder, B.Cu at (148.5, 117.5)
- added REF**30: R_1206_3216Metric_Pad1.30x1.75mm_HandSolder, Resistor_SMD:R_1206_3216Metric_Pad1.30x1.75mm_HandSolder, B.Cu at (148.5, 108.9)
- added REF**31: R_1206_3216Metric_Pad1.30x1.75mm_HandSolder, Resistor_SMD:R_1206_3216Metric_Pad1.30x1.75mm_HandSolder, B.Cu at (156.5, 117.5)
- added REF**32: R_1206_3216Metric_Pad1.30x1.75mm_HandSolder, Resistor_SMD:R_1206_3216Metric_Pad1.30x1.75mm_HandSolder, B.Cu at (156.5, 108.9)
- moved G*** 1.00 mm to (200.0, 155.0)
- moved G*** 1.00 mm to (123.1, 106.6)
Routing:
- net -12: track 28.6 -> 370.7 mm
- net +12: track 41.9 -> 355.8 mm
- net Net-(J2-In): track 17.5 -> 0.00 mm
- net Net-(D4-A): track 12.3 -> 0.00 mm
- net +11: track 11.0 -> 0.00 mm
- net Net-(J3-In): track 11.0 -> 0.00 mm
- net -11: track 10.4 -> 0.00 mm
- net Net-(Q2-E): track 9.88 -> 0.00 mm
- net Net-(D3-K): track 8.85 -> 0.00 mm
- net Net-(J4-Pin_4): track 6.66 -> 0.00 mm
- net Net-(J4-Pin_3): track 6.49 -> 0.00 mm
- net Net-(Q1-E): track 5.61 -> 0.00 mm
- net GND: track 4.00 -> 0.00 mm, vias 2 -> 1
- net (no net): vias 2 -> 0
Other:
- board size 251 x 152 mm -> 177 x 152 mm
- board text removed: "in"
- board text removed: "out"
